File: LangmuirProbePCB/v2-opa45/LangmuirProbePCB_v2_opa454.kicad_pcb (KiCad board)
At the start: 2 copper layers, 25.2 x 32.2 mm, 10 parts, among them U1 OPA454

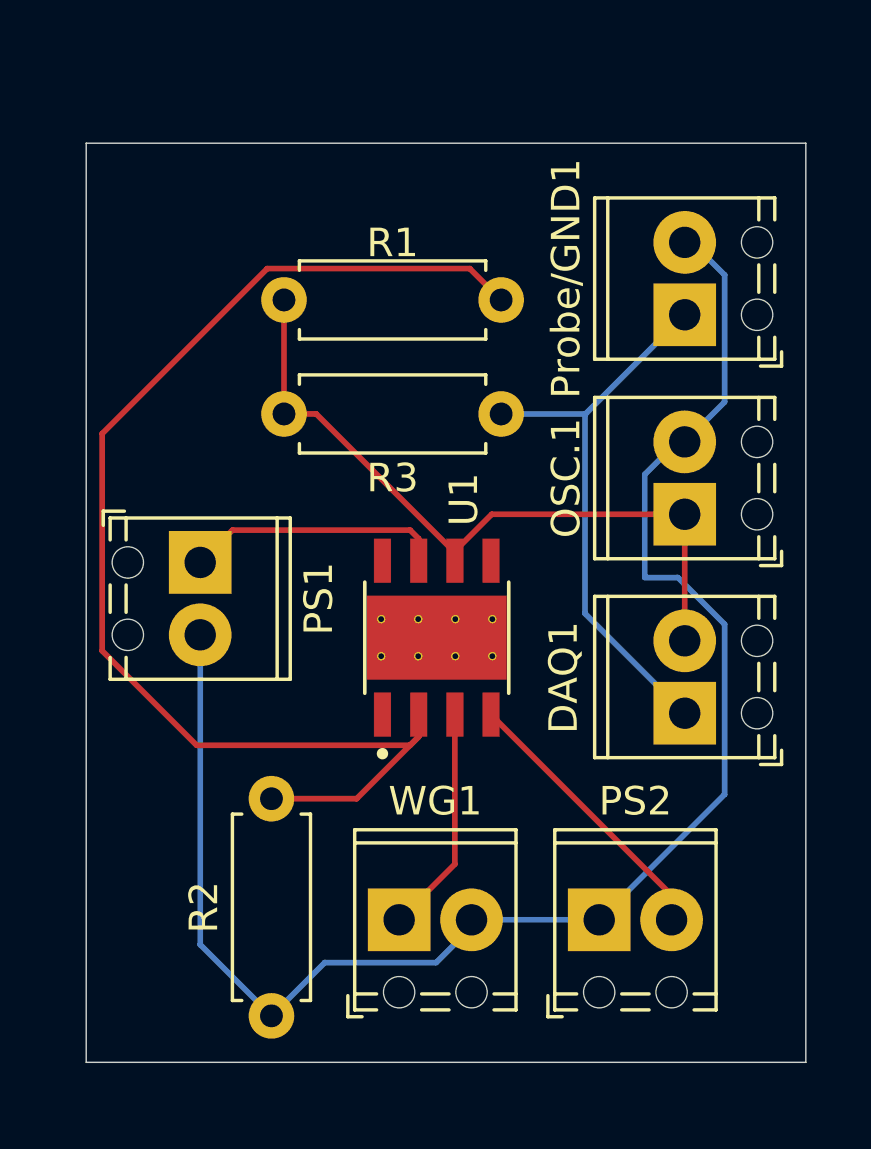
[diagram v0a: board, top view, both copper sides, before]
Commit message: added mounting holes
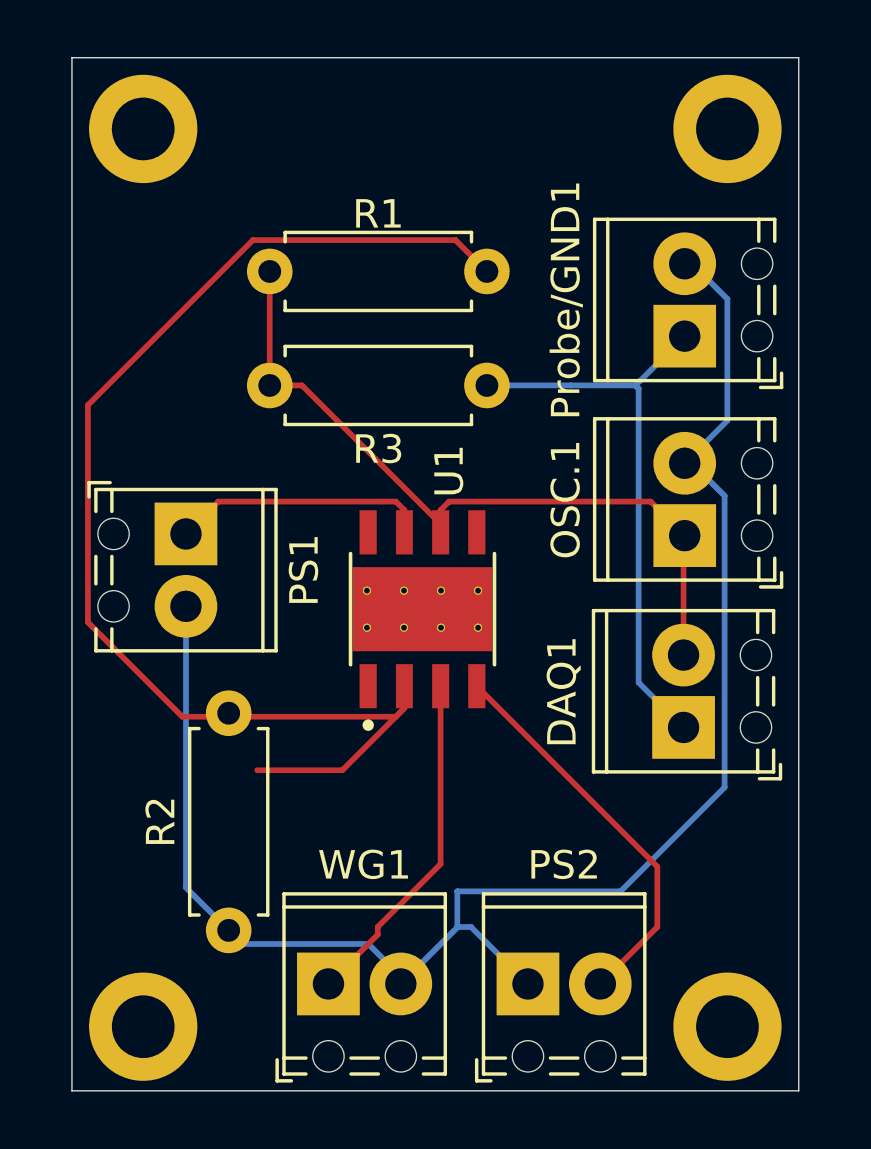
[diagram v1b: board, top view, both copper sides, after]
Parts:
- added REF**: MountingHole_2.2mm_M2_DIN965_Pad, MountingHole:MountingHole_2.2mm_M2_DIN965_Pad, F.Cu at (83.0, 42.5)
- added REF**: MountingHole_2.2mm_M2_DIN965_Pad, MountingHole:MountingHole_2.2mm_M2_DIN965_Pad, F.Cu at (83.0, 74.0)
- added REF**: MountingHole_2.2mm_M2_DIN965_Pad, MountingHole:MountingHole_2.2mm_M2_DIN965_Pad, F.Cu at (62.5, 74.0)
- added REF**: MountingHole_2.2mm_M2_DIN965_Pad, MountingHole:MountingHole_2.2mm_M2_DIN965_Pad, F.Cu at (62.5, 42.5)
- moved PS2 3.36 mm to (76.0, 72.5)
- moved R2 3.35 mm to (65.5, 70.6)
- moved WG1 3.35 mm to (69.0, 72.5)
- moved PS1 1.12 mm to (64.0, 56.7)
- moved R1 1.12 mm to (74.6, 47.5)
- moved R3 1.12 mm to (66.9, 51.5)
- moved U1 1.12 mm to (72.3, 59.4)
- moved OSC.1 0.75 mm to (81.5, 56.8)
- moved Probe/GND1 0.75 mm to (81.5, 49.8)
- moved DAQ1 0.50 mm to (81.5, 63.5)
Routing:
- net Net-(PS2-Pin_2): track 9.82 -> 13.9 mm
- net Net-(U1-+): track 8.01 -> 12.1 mm
- net Net-(OSC.1-Pin_2): track 56.9 -> 58.7 mm
- net Net-(DAQ1-Pin_2): track 25.7 -> 26.5 mm
- net Net-(DAQ1-Pin_1): track 19.8 -> 20.4 mm
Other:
- board size 25.2 x 32.2 mm -> 25.5 x 36.2 mm

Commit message: board final
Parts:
- moved REF** 0.50 mm to (83.5, 42.5)
- moved REF** 0.50 mm to (83.5, 74.0)
- moved REF** 0.50 mm to (62.0, 74.0)
- moved REF** 0.50 mm to (62.0, 42.5)
- renumbered DAQ1 to DAQ, OSC.1 to OSC, Probe/GND1 to Probe/GND
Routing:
- net Net-(U1--): track 43.9 -> 39.9 mm
- net Net-(OSC.1-Pin_2): track 58.7 -> 61.3 mm
- net Net-(PS2-Pin_2): track 13.9 -> 12.2 mm
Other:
- board size 25.5 x 36.2 mm -> 26.5 x 36.2 mm

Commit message: usc aspen
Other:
- board text added: "USC ASPEN"
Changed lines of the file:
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@@
 		(layer "Edge.Cuts")
+	)
+	(gr_text "USC ASPEN"
+		(at 64.174734 43.506718 -0)
+		(layer "F.Cu")
+		(effects
+			(font
+				(size 2 2)
+				(thickness 0.3)
+				(bold yes)
+			)
+			(justify left bottom)
+		)
+	)
+	(gr_text "USC ASPEN"
+		(at 81.5 43.5 0)
+		(layer "B.Cu")
+		(effects
+			(font
+				(size 2 2)
+				(thickness 0.3)
+				(bold yes)
+			)
+			(justify left bottom mirror)
+		)
 	)
 	(segment

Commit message: removing unnecessary numbers to make me happy
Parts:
- renumbered WG1 to WG
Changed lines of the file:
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@@
 		(descr "Terminal Block Phoenix MPT-0,5-2-2.54, 2 pins, pitch 2.54mm, size 5.54x6.2mm^2, drill diamater 1.1mm, pad diameter 2.2mm, see http://www.mouser.com/ds/2/324/ItemDetail_1725656-920552.pdf, script-generated using https://github.com/pointhi/kicad-footprint-generator/scripts/TerminalBlock_Phoenix")
 		(tags "THT Terminal Block Phoenix MPT-0,5-2-2.54 pitch 2.54mm size 5.54x6.2mm^2 drill 1.1mm pad 2.2mm")
-		(property "Reference" "WG1"
+		(property "Reference" "WG"
 			(at 1.27 -4.16 0)
 			(layer "F.SilkS")
